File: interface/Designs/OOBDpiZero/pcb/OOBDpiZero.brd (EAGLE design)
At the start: 65 x 30 mm, 62 parts, among them IC3 DS3231, U1 SN65HVD230(SO8), U2 SN65HVD230(SO8), U5 MP1482

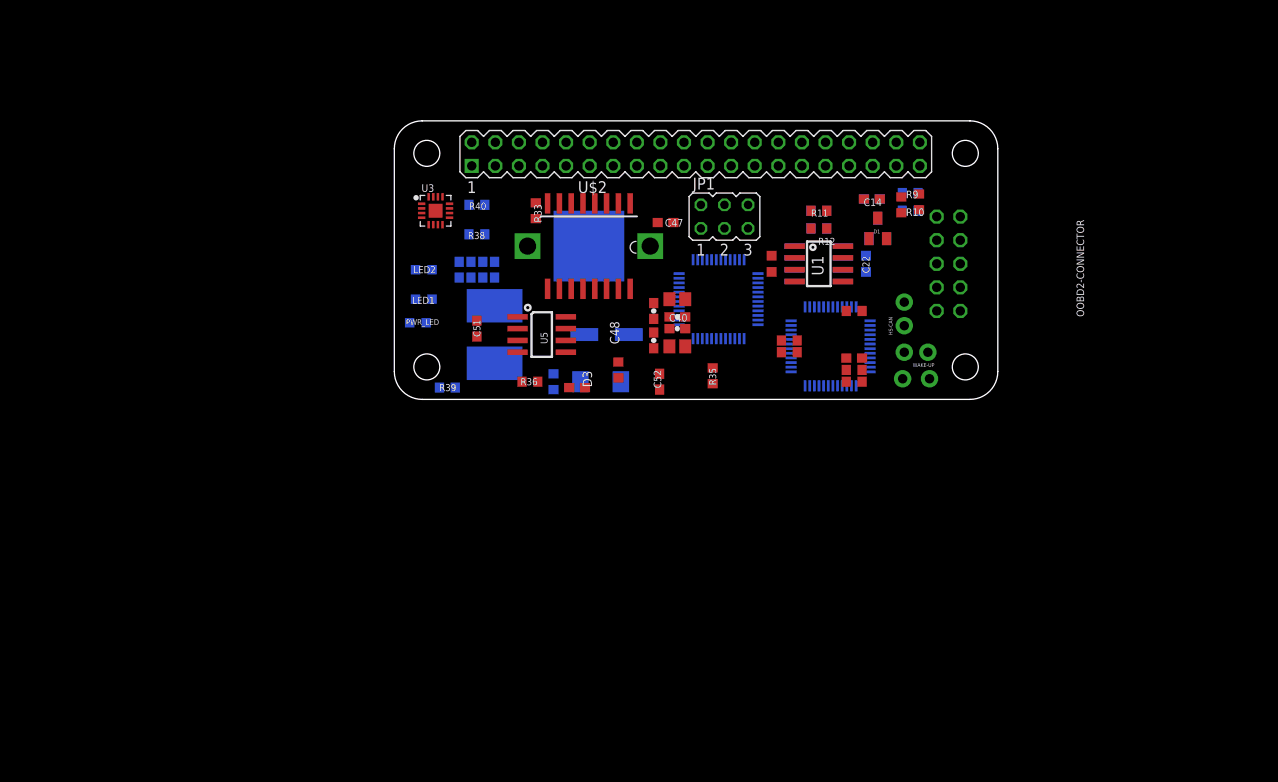
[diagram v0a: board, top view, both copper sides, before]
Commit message: modify OOBpiZero due to schematic review
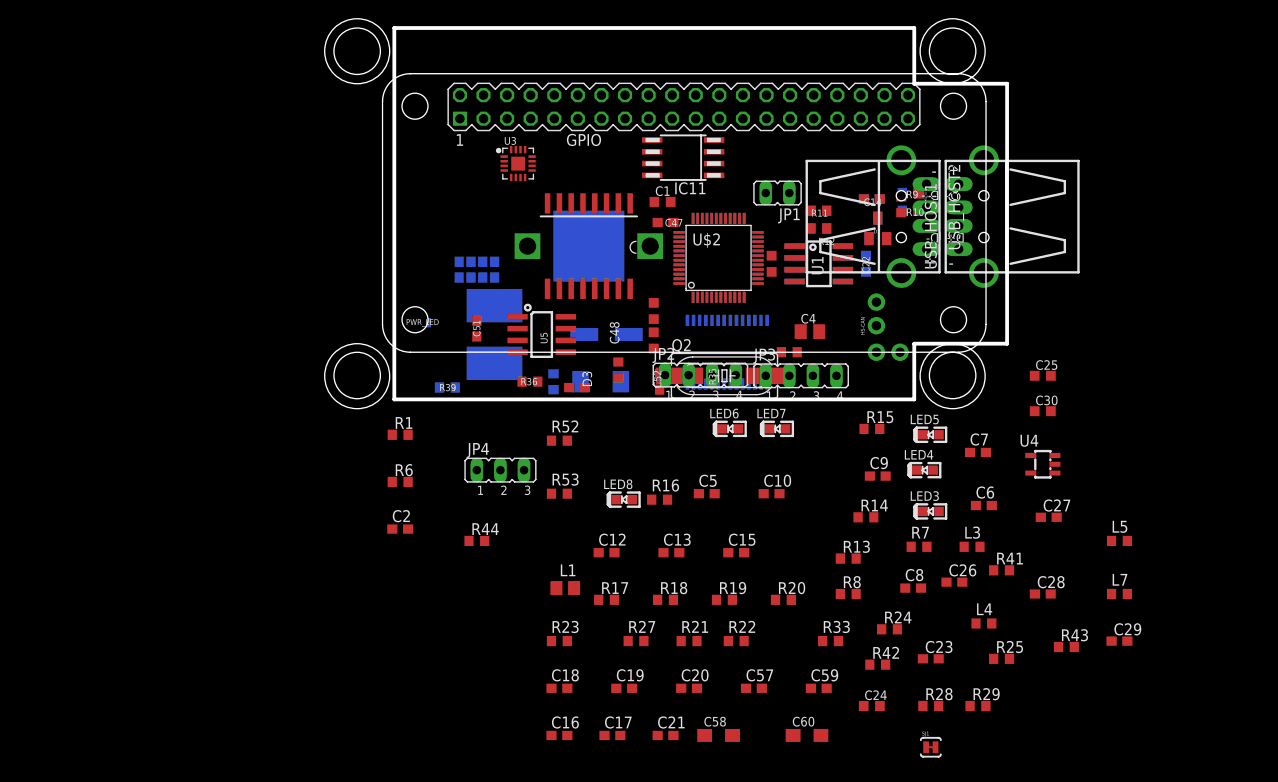
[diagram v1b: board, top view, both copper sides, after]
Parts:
- removed C39: 22µF, SparkFun-Passives:0603-CAP
- removed C40: 0.1µF, SparkFun-Passives:0603-CAP
- removed C49: 100nF, rcl:C0603
- removed LED1: LED/Yellow/0603, DOUBLE-SIDE:LED_0603
- removed LED2: LED/Red/0603, DOUBLE-SIDE:LED_0603
- removed OOBD2-CONNECTOR: In-Car Diagnostic, pinhead:2X05/90
- removed R30, R38, R40: 2.2k/1%, rcl:R0603
- removed R31: NI, rcl:R0603
- removed R34: 49.9R/1%, rcl:R0603
- removed U$4: STM32F042CT, micro-stm_v3:LQFP48
- removed WAKE-UP: Open, SparkFun:1X02_LOCK
- added C1, C24, C25, C30: 100nF, rcl:C0603K
- added C10, C12, C13, C15, C18, C19, C2, C20, C5, C57, C59, C6, C7, C8, C9: 100nF, resistor:C0603
- added C16, C17: 33pF, resistor:C0603
- added C21: 1uF, resistor:C0603
- added C23: 100nF, rcl:C0603
- added C26, C27, C28, C29: 22uF/6.3V, rcl:C0603
- added C4: 10uF, rcl:C0805K
- added C58, C60: 22uF/6.3V, rcl:SMC_A
- added GPIO: PIZERO_THROUGH_HOLE, pizero:PIZERO_THOUGH_HOLE
- added IC11: EEPROM24, FLYFISH:SOIC8
- added JP2, JP3: (no value), jumper:JP4
- added JP4: (no value), jumper:JP2
- added L1: 2508056017Y2, rcl:L0805@1
- added L3, L4, L5, L7: FB0805/600R/2A, rcl:L0603
- added LED3, LED6: gr, DOUBLE-SIDE:LED_0603
- added LED4, LED7: yel, DOUBLE-SIDE:LED_0603
- added LED5, LED8: red, DOUBLE-SIDE:LED_0603
- added Q2: 12MHz, crystal:SM49
- added R1, R25, R41, R6: 10k, rcl:R0603
- added R13, R14, R15, R17, R18, R19, R20, R8: 330R, rcl:R0603
- added R16, R7: 60R, resistor:R0603
- added R21, R22: 10k, resistor:R0603
- added R23: NA(47k), resistor:R0603
- added R24: 6k8k/1%, rcl:R0603
- added R42: 2.2k/1%, rcl:R0603
- added R43, R44: NI, rcl:R0603
- added R52, R53: NI, resistor:R0603
- added SJ1: SOLDERJUMPERTRACE, SparkFun:SJ_2S-TRACE
- added U$5: GL850G-31, pimoroni:TSSOP28
- added U4: SY6280, OLIMEX_IC:SOT23-5
- added USB_HOST1, USB_HOST2: USB_A_VERTICAL, OLIMEX_CONNECTORS:USB_PN87520_DEV_PTH
- C45, C46: value NI (0,01µF) -> 220pF; device SparkFun-Passives:0603-CAP -> rcl:C0603K
- JP1: value Audio-Out -> (none); device jumper:JP3Q -> jumper:JP1
- R26: value 10K -> 1M
- R27: value 10K -> 680R
- R28, R29: value 0R -> 10k; device resistor:R0805 -> rcl:R0603
- R33: device rcl:R0603 -> resistor:R0603
- U$2: value PIZERO_THROUGH_HOLE -> STM32F042CT; device pizero:PIZERO_THOUGH_HOLE -> micro-stm_v3:LQFP48
- moved R33 56.2 mm to (47.0, -26.0), turned to 0 degrees
- moved R29 54.5 mm to (62.9, -33.0), turned to 0 degrees
- moved R28 47.4 mm to (57.8, -33.0), turned to 0 degrees
- moved U$2 38.1 mm to (34.9, 15.2)
- moved R27 36.4 mm to (26.0, -26.0)
- moved U3 10.2 mm to (13.3, 25.4)
- moved JP1 6.25 mm to (41.3, 22.2), turned to 90 degrees
- moved U$3 4.45 mm to (34.9, 15.2)
- moved HS-CAN 3.00 mm to (51.9, 7.94)
- moved MS-CAN 3.00 mm to (51.9, 5.08)
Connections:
- removed net AGND: C45.1, C46.1, JP1.5
- removed net DCAN0_RX: U2.4
- removed net DCAN0_TX: U2.1
- removed net DCAN1_RX: U1.4
- removed net DCAN1_TX: U1.1
- removed net EXT_WAKEUP: R34.1
- removed net I2C0-SCL: IC3.16, R26.1
- removed net I2C0-SDA: IC3.15, R27.1
- removed net LED1: R38.1
- removed net LED2: R40.1
- removed net N$1: LED2.A, R40.2
- removed net N$231: LED1.A, R38.2
- removed net N$43: R30.1, WAKE-UP.1
- removed net N$44: C49.1, R31.1, R34.2, WAKE-UP.2
- removed net SYS_RESETN: IC3.4
- removed net VDD: U3.7, U3.8
- removed net VDD1: U$3.24, U$4.24
- removed net VDD2: U$3.48, U$4.48
- removed net VDDA: U$3.9, U$4.9
- removed net VDDIO2: U$3.36, U$4.36
- removed net VSS1: U$3.23, U$4.23
- removed net VSS2: U$3.35, U$4.35
- removed net VSS3: U$3.47, U$4.47
- removed net VSSA: U$3.8, U$4.8
- new net AUD_BCLK: GPIO.18, U3.16
- new net AUD_DIN: GPIO.21, U3.1
- new net AUD_LRCLK: GPIO.19, U3.14
- new net AUD_SD_MODE: GPIO.29, R26.1, U3.4
- new net HS-CAN_RXD: U$3.45, U1.4
- new net HS-CAN_TXD: U$3.46, U1.1
- new net ID_SC: GPIO.28, IC11.6, R29.2
- new net ID_SD: GPIO.27, IC11.5, R25.2
- new net MS-CAN_RXD: U$2.45, U2.4
- new net MS-CAN_TXD: U$2.46, U2.1
- new net N$12: C46.2, JP1.1, U3.9
- new net N$13: R8.2, U$3.10
- new net N$17: LED5.C, R14.1
- new net N$18: LED4.C, R13.1
- new net N$20: C9.2, R15.2, U$3.7
- new net N$21: R16.1, U$2.44
- new net N$22: R17.2, U$2.10
- new net N$23: R18.2, U$2.11
- new net N$24: R19.2, U$2.12
- new net N$25: LED8.C, R19.1
- new net N$26: LED7.C, R18.1
- new net N$28: C15.2, R20.2, U$2.7
- new net N$29: C17.1, Q2.2, U$5.7
- new net N$3: C45.2, JP1.2, U3.10
- new net N$31: C16.1, Q2.1, U$5.6
- new net N$33: C57.1, C58.+, L1.2, R21.2, R33.2, U$5.16, U$5.24
- new net N$34: R33.1, U$5.18
- new net N$35: R21.1, U$5.17
- new net N$36: C21.1, R22.2, R23.2, U$5.13
- new net N$37: R52.2, R53.1, U3.2
- new net N$39: C18.1, C19.1, C20.1, L1.1, U$5.1, U$5.10, U$5.5
- new net N$40: R27.2, U$5.4
- new net N$41: C24.1, L4.2, USB_HOST1.1
- new net N$42: L3.2, USB_HOST1.P$1, USB_HOST1.P$2
- new net N$45: R24.2, U4.3
- new net N$46: IC11.7, R28.2, SJ1.2
- new net N$47: C26.1, C27.1, C28.1, C29.1, L4.1, L5.1, R42.2, U4.1
- new net N$48: C25.1, L5.2, USB_HOST2.1
- new net N$49: L7.2, USB_HOST2.P$1, USB_HOST2.P$2
- new net PP22: U$5.26
- new net PP23: U$5.25
- new net SCL: GPIO.5, IC3.16, R1.2
- new net SDA: GPIO.3, IC3.15, R6.2
- new net SWCLK: JP2.3, JP3.3, U$2.37, U$3.37
- new net SWDIO: JP2.2, JP3.2, U$2.34, U$3.34
- new net UART0_RXD: GPIO.10, JP4.2
- new net UART0_TXD: GPIO.8, JP4.1
- new net USB0_DM: U$3.32, U$5.27
- new net USB0_DP: U$3.33, U$5.28
- new net USB1_DM: U$2.32, U$5.2
- new net USB1_DP: U$2.33, U$5.3
- new net USB1_EN: R41.2, R43.1, R44.1, U4.4
- new net USB2_DM: U$5.8, USB_HOST1.2
- new net USB2_DP: U$5.9, USB_HOST1.3
- new net USB3_DM: U$5.11, USB_HOST2.2
- new net USB3_DP: U$5.12, USB_HOST2.3
- new net USB_CE: GPIO.31, R43.2
- new net USB_VBUS: GPIO.32, R42.1
- net +12V: no longer OOBD2-CONNECTOR.10
- net +3V3: now also C10.2, C12.2, C13.2, C2.2, C5.2, C6.2, C7.2, C8.2, GPIO.1, GPIO.17, JP2.1, JP3.1, LED3.A, LED4.A, LED5.A, LED6.A, LED7.A, LED8.A, R1.1, R15.1, R20.1, R44.2, R6.1, U$2.1, U$2.24, U$2.36, U$2.48, U$2.9, U$3.1, U$3.24, U$3.36, U$3.48, U$3.9; no longer R26.2, R27.2, R30.2, R33.2
- net +5V: now also C1.1, C23.2, C30.1, C4.1, C59.1, C60.+, GPIO.2, GPIO.4, IC11.8, R22.1, R25.1, R26.2, R28.1, R29.1, R53.2, U$5.23, U3.7, U3.8, U4.5; no longer C39.2, C40.2
- net GND: now also C1.2, C10.1, C12.1, C13.1, C15.1, C16.2, C17.2, C18.2, C19.2, C2.1, C20.2, C21.2, C23.1, C24.2, C25.2, C26.2, C27.2, C28.2, C29.2, C30.2, C4.2, C45.1, C46.1, C5.1, C57.2, C58.-, C59.2, C6.1, C60.-, C7.1, C8.1, C9.1, GPIO.14, GPIO.20, GPIO.25, GPIO.30, GPIO.34, GPIO.39, GPIO.6, GPIO.9, IC11.1, IC11.2, IC11.3, IC11.4, JP2.4, JP3.4, JP4.3, L3.1, L7.1, R16.2, R23.1, R24.1, R27.1, R41.1, R52.1, R7.2, SJ1.1, U$2.23, U$2.35, U$2.47, U$2.8, U$3.23, U$3.35, U$3.47, U$3.8, U$5.14, U$5.15, U4.2, USB_HOST1.4, USB_HOST2.4; no longer C39.1, C40.1, C49.2, JP1.6, LED1.C, LED2.C, OOBD2-CONNECTOR.3, R31.2
- net HS-CAN_H: no longer OOBD2-CONNECTOR.7
- net HS-CAN_L: no longer OOBD2-CONNECTOR.6
- net HS-CAN_RS: now also GPIO.35
- net MS-CAN_H: no longer OOBD2-CONNECTOR.1
- net MS-CAN_L: no longer OOBD2-CONNECTOR.2
- net MS-CAN_RS: now also GPIO.36
- net N$14: now also R13.2, U$3.11; no longer JP1.1
- net N$15: now also R7.1, U$3.44; no longer C45.2, JP1.4, R29.2
- net N$16: now also R14.2, U$3.12; no longer C46.2, JP1.2, R28.2
- net N$19: now also LED3.C, R8.1; no longer JP1.3
- net N$27: now also LED6.C, R17.1; no longer IC3.3, R33.1
- net VBAT: no longer U$3.1, U$4.1
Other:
- board size 65 x 30 mm -> 73.5 x 42 mm

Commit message: exchange power supply circuit to MC34063
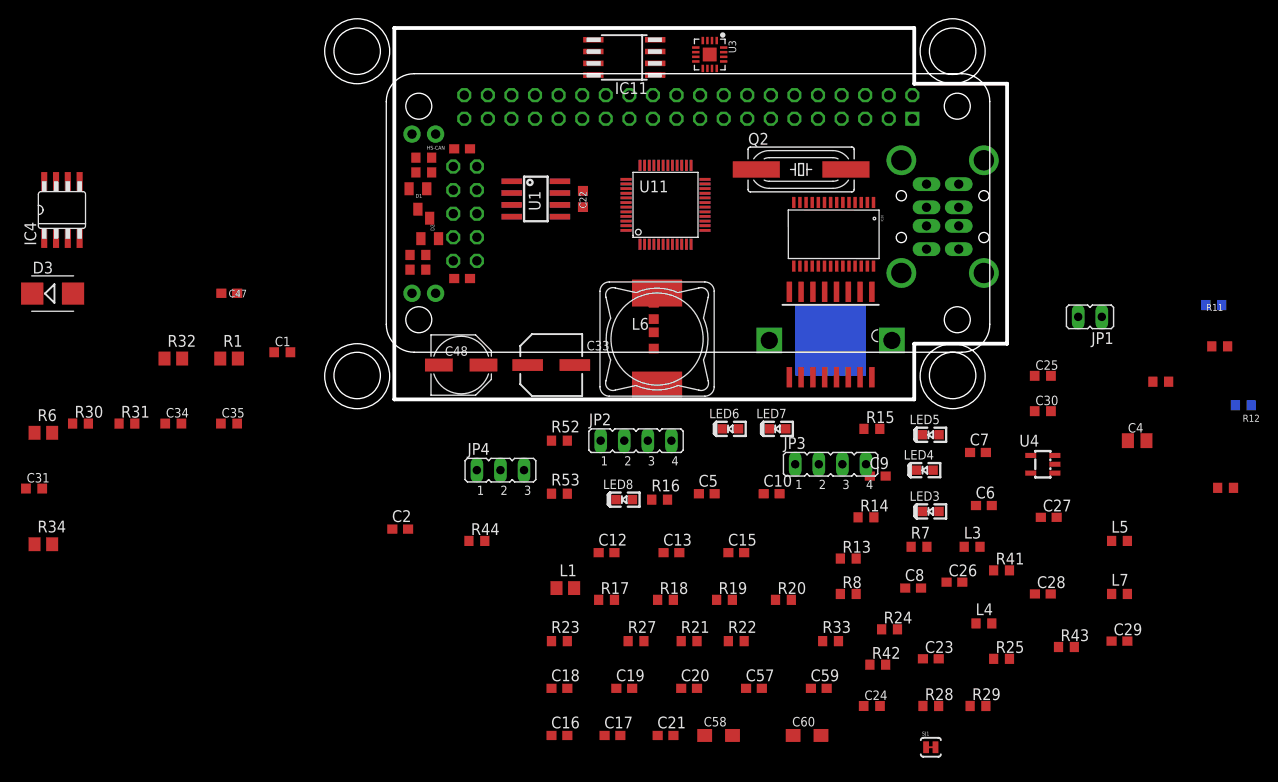
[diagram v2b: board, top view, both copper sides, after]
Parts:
- removed C50: 100nF, rcl:C0603
- removed C51: 10nF, rcl:C0603
- removed C52: 3.3nF, rcl:C0603
- removed C53, C54, C55, C56: 22uF/6.3V, rcl:C0603
- removed GPIO: PIZERO_THROUGH_HOLE, pizero:PIZERO_THOUGH_HOLE
- removed PWR_LED: LED/Red/0603, DOUBLE-SIDE:LED-0603
- removed R35, R39: 2.2k/1%, rcl:R0603
- removed R36: 1.05k/1%, rcl:R0603
- removed R37: 4.99k/1%, rcl:R0603
- removed U$2, U$3: STM32F042CT, micro-stm_v3:LQFP48
- removed U$5: GL850G-31, pimoroni:TSSOP28
- removed U5: MP1482, OLIMEX_IC:SOIC8
- added C31: 100n, rcl:C0603K
- added C33: 47µ/35V, cap-master:SV-D
- added C34: 100nF, rcl:C0603K
- added C35: 220pF, rcl:C0603K
- added IC10, U11: STM32F042CT, micro-stm_v3:LQFP48
- added IC20: GL850G-31, pimoroni:TSSOP28
- added IC4: MC34063-SO, mc34063:SO8
- added JP7: PIZERO_THROUGH_HOLE, pizero:PIZERO_THOUGH_HOLE
- added OOBD2-CONNECTOR: In-Car Diagnostic, pinhead:2X05/90
- added R30: 1k2, rcl:R0603
- added R31: 3k6, rcl:R0603
- added R34: 1R, rcl:R0805
- C48: value 470uF/25V/LOWESR/105C -> 220uF/10V/LOWESR/105C
- D3: value SMBJ16A -> SK24; device OLIMEX_DISCRET:DO214AA -> diode:SMB
- L6: value 10uH/3.15A/20% -> 100uH; device OLIMEX_DISCRET:8X8MM_3131 -> Inductor-Fastron:PIS4720
- R1, R32, R6: value 10k -> 1R; device rcl:R0603 -> rcl:R0805
- moved D3 59.8 mm to (-36.8, 11.4), flipped to the top
- moved R3 53.6 mm to (3.17, 26.0), turned to 180 degrees
- moved R9 53.4 mm to (2.54, 15.6), flipped to the top, turned to 180 degrees
- moved R10 53.4 mm to (2.54, 14.0), flipped to the top, turned to 180 degrees
- moved HS-CAN 51.8 mm to (4.45, 28.6), turned to 0 degrees
- moved R2 51.6 mm to (3.17, 24.4), turned to 180 degrees
- moved D1 49.6 mm to (2.54, 21.6), turned to 180 degrees
- moved R12 49.5 mm to (91.4, -0.64)
- moved R26 49.2 mm to (89.5, -9.53)
- moved D2 48.3 mm to (3.81, 18.4), flipped to the top
- moved R32 47.9 mm to (-23.8, 4.40), turned to 0 degrees
- moved MS-CAN 47.9 mm to (4.45, 11.4), turned to 0 degrees
- moved C47 47.6 mm to (-17.8, 11.4)
- moved R5 45.0 mm to (88.9, 5.71)
- moved C14 45.0 mm to (7.30, 13.0), flipped to the top, turned to 0 degrees
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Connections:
- removed net N$129: PWR_LED.A, R39.2
- removed net N$62: R36.1, R37.1, U5.5
- removed net N$7: C51.1, U5.1
- removed net N$8: C51.2, L6.1, U5.3
- removed net N$9: C52.1, U5.6
- new net N$1: IC4.1, IC4.7, IC4.8, R1.1, R32.1, R34.1, R6.1
- net +12V: now also C33.+, C34.1, IC4.6, OOBD2-CONNECTOR.10, R1.2, R32.2, R34.2, R6.2; no longer C48.+, D3.C, R32.1, U5.2
- net +3V3: now also IC10.1, IC10.24, IC10.36, IC10.48, IC10.9, JP7.1, JP7.17, U11.1, U11.24, U11.36, U11.48, U11.9; no longer GPIO.1, GPIO.17, R1.1, R6.1, U$2.1, U$2.24, U$2.36, U$2.48, U$2.9, U$3.1, U$3.24, U$3.36, U$3.48, U$3.9
- net +5V: now also C31.1, C48.+, IC20.23, JP7.2, JP7.4, L6.P$1, R31.2; no longer C53.1, C54.1, C55.1, C56.1, GPIO.2, GPIO.4, L6.2, R37.2, R39.1, U$5.23
- net AUD_BCLK: now also JP7.18; no longer GPIO.18
- net AUD_DIN: now also JP7.21; no longer GPIO.21
- net AUD_LRCLK: now also JP7.19; no longer GPIO.19
- net AUD_SD_MODE: now also JP7.29; no longer GPIO.29
- net GND: now also C31.2, C33.-, C34.2, C35.2, IC10.23, IC10.35, IC10.47, IC10.8, IC20.14, IC20.15, IC4.4, JP7.14, JP7.20, JP7.25, JP7.30, JP7.34, JP7.39, JP7.6, JP7.9, OOBD2-CONNECTOR.3, R30.2, U11.23, U11.35, U11.47, U11.8; no longer C50.2, C53.2, C54.2, C55.2, C56.2, GPIO.14, GPIO.20, GPIO.25, GPIO.30, GPIO.34, GPIO.39, GPIO.6, GPIO.9, PWR_LED.C, R35.2, R36.2, U$2.23, U$2.35, U$2.47, U$2.8, U$3.23, U$3.35, U$3.47, U$3.8, U$5.14, U$5.15, U5.4
- net HS-CAN_H: now also OOBD2-CONNECTOR.7
- net HS-CAN_L: now also OOBD2-CONNECTOR.6
- net HS-CAN_RS: now also JP7.35; no longer GPIO.35
- net HS-CAN_RXD: now also IC10.45; no longer U$3.45
- net HS-CAN_TXD: now also IC10.46; no longer U$3.46
- net ID_SC: now also JP7.28; no longer GPIO.28
- net ID_SD: now also JP7.27; no longer GPIO.27
- net MS-CAN_H: now also OOBD2-CONNECTOR.1
- net MS-CAN_L: now also OOBD2-CONNECTOR.2
- net MS-CAN_RS: now also JP7.36; no longer GPIO.36
- net MS-CAN_RXD: now also U11.45; no longer U$2.45
- net MS-CAN_TXD: now also U11.46; no longer U$2.46
- net N$11: now also C35.1, IC4.3; no longer C52.2, R35.1
- net N$13: now also IC10.10; no longer U$3.10
- net N$14: now also IC10.11; no longer U$3.11
- net N$15: now also IC10.44; no longer U$3.44
- net N$16: now also IC10.12; no longer U$3.12
- net N$20: now also IC10.7; no longer U$3.7
- net N$21: now also U11.44; no longer U$2.44
- net N$22: now also U11.10; no longer U$2.10
- net N$23: now also U11.11; no longer U$2.11
- net N$24: now also U11.12; no longer U$2.12
- net N$28: now also U11.7; no longer U$2.7
- net N$29: now also IC20.7; no longer U$5.7
- net N$31: now also IC20.6; no longer U$5.6
- net N$33: now also IC20.16, IC20.24; no longer U$5.16, U$5.24
- net N$34: now also IC20.18; no longer U$5.18
- net N$35: now also IC20.17; no longer U$5.17
- net N$36: now also IC20.13; no longer U$5.13
- net N$39: now also IC20.1, IC20.10, IC20.5; no longer U$5.1, U$5.10, U$5.5
- net N$4: now also IC4.5, R30.1, R31.1; no longer C50.1, U5.8
- net N$40: now also IC20.4; no longer U$5.4
- net N$6: now also D3.C, IC4.2, L6.P$2; no longer R32.2, U5.7
- net PP22: now also IC20.26; no longer U$5.26
- net PP23: now also IC20.25; no longer U$5.25
- net SCL: now also JP7.5; no longer GPIO.5, R1.2
- net SDA: now also JP7.3; no longer GPIO.3, R6.2
- net SWCLK: now also IC10.37, U11.37; no longer U$2.37, U$3.37
- net SWDIO: now also IC10.34, U11.34; no longer U$2.34, U$3.34
- net UART0_RXD: now also JP7.10; no longer GPIO.10
- net UART0_TXD: now also JP7.8; no longer GPIO.8
- net USB0_DM: now also IC10.32, IC20.27; no longer U$3.32, U$5.27
- net USB0_DP: now also IC10.33, IC20.28; no longer U$3.33, U$5.28
- net USB1_DM: now also IC20.2, U11.32; no longer U$2.32, U$5.2
- net USB1_DP: now also IC20.3, U11.33; no longer U$2.33, U$5.3
- net USB2_DM: now also IC20.8; no longer U$5.8
- net USB2_DP: now also IC20.9; no longer U$5.9
- net USB3_DM: now also IC20.11; no longer U$5.11
- net USB3_DP: now also IC20.12; no longer U$5.12
- net USB_CE: now also JP7.31; no longer GPIO.31
- net USB_VBUS: now also JP7.32; no longer GPIO.32
